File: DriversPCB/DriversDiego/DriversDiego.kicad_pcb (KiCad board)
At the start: 2 copper layers, 100 x 60 mm, 35 parts, among them IC1 DRV8411PWPR, IC2 DRV8411PWPR, IC3 DRV8411PWPR, J1 TB0012-508-02GR, J10 TB0012-508-02GR, J11 TB0012-508-02GR, J12 TB0012-508-02GR, J13 TB0012-508-02GR, J14 TB0012-508-02GR, J15 TB0012-508-02GR, J16 TB0012-508-02GR, J17 TB0012-508-02GR, J18 TB0012-508-02GR, J19 TB0012-508-02GR, J2 TB0012-508-02GR, J3 TB0012-508-02GR, J4 TB0012-508-02GR, J5 TB0012-508-02GR, J6 TB0012-508-02GR, J7 TB0012-508-02GR, J8 TB0012-508-02GR, J9 TB0012-508-02GR, U1 DRV8871DDA

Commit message: Zona cobre...
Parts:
- C1: footprint WCAP-CSGP_0805_H1.25:WCAP-CSGP_0805_H1.25_R -> Kicad_TitoSync_Footprints:WCAP-CSGP_0805_H1.25_R
- C3: footprint CL21B106KOQNFNE:CAPC2012X140N -> Kicad_TitoSync_Footprints:CAPC2012X140N
- IC1, IC2, IC3: footprint DRV8411PWPR:PWP0016C-IPC_A -> Kicad_TitoSync_Footprints:PWP0016C-IPC_A
- moved J14 93.2 mm to (115.0, 156.5), turned to 0 degrees
- moved J9 89.5 mm to (106.0, 133.0), turned to 90 degrees
- moved J15 80.6 mm to (193.5, 149.5), turned to -90 degrees
- moved J8 79.9 mm to (119.0, 104.5), turned to 0 degrees
- moved J19 76.2 mm to (180.0, 155.5), turned to 180 degrees
- moved J10 74.7 mm to (131.5, 104.0), turned to 0 degrees
- moved J6 73.2 mm to (128.0, 155.5)
- moved J4 63.2 mm to (106.5, 120.5), turned to -90 degrees
- moved J18 62.4 mm to (167.0, 155.5)
- moved J16 56.1 mm to (193.5, 137.0), turned to -90 degrees
- moved J5 55.9 mm to (154.0, 155.5), turned to 0 degrees
- moved J17 51.7 mm to (141.0, 155.5), turned to 0 degrees
- moved C3 51.6 mm to (114.6, 122.1), turned to -90 degrees
- moved J12 50.0 mm to (193.5, 124.0), turned to -90 degrees
- moved J11 48.6 mm to (169.5, 105.5)
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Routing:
- net Net-(IC1-VM): track 178.7 -> 104.2 mm, vias 0 -> 6
- net Net-(IC1-SLEEP_N): track 79.0 -> 11.6 mm
- net Net-(IC1-AOUT2): track 55.8 -> 20.4 mm
- net Net-(IC2-SLEEP_N): track 79.6 -> 49.1 mm, vias 0 -> 3
- net Net-(U1-OUT1): track 24.1 -> 53.4 mm, vias 0 -> 1
- net Net-(IC1-BOUT1): track 65.2 -> 39.2 mm, vias 0 -> 1
- net Net-(IC1-BOUT2): track 59.0 -> 33.6 mm, vias 0 -> 1
- net Net-(IC3-AIN2): track 13.9 -> 38.5 mm, vias 0 -> 1
- net Net-(IC2-BOUT1): track 23.9 -> 46.9 mm, vias 0 -> 1
- net Net-(U1-OUT2): track 28.8 -> 51.7 mm, vias 0 -> 2
- net Net-(IC3-SLEEP_N): track 58.8 -> 36.1 mm, vias 0 -> 3
- net Net-(IC3-AIN1): track 15.7 -> 36.1 mm, vias 0 -> 1
- net Net-(IC1-FAULT_N): track 44.9 -> 24.7 mm, vias 0 -> 1
- net Net-(IC3-AOUT2): track 27.0 -> 46.5 mm
- net Net-(IC1-BIN1): track 42.6 -> 24.3 mm
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- added copper zone on B.Cu, net GND

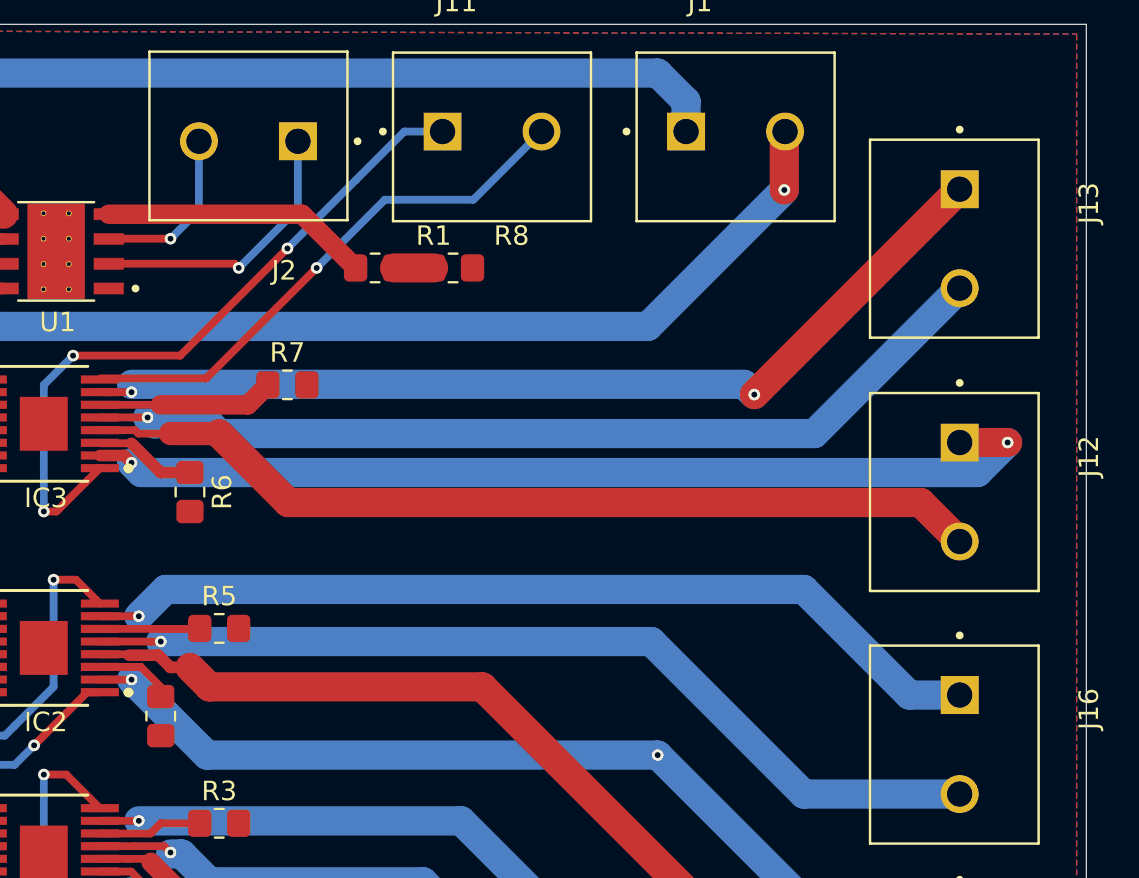
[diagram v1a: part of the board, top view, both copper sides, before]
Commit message: Driver PCB complete
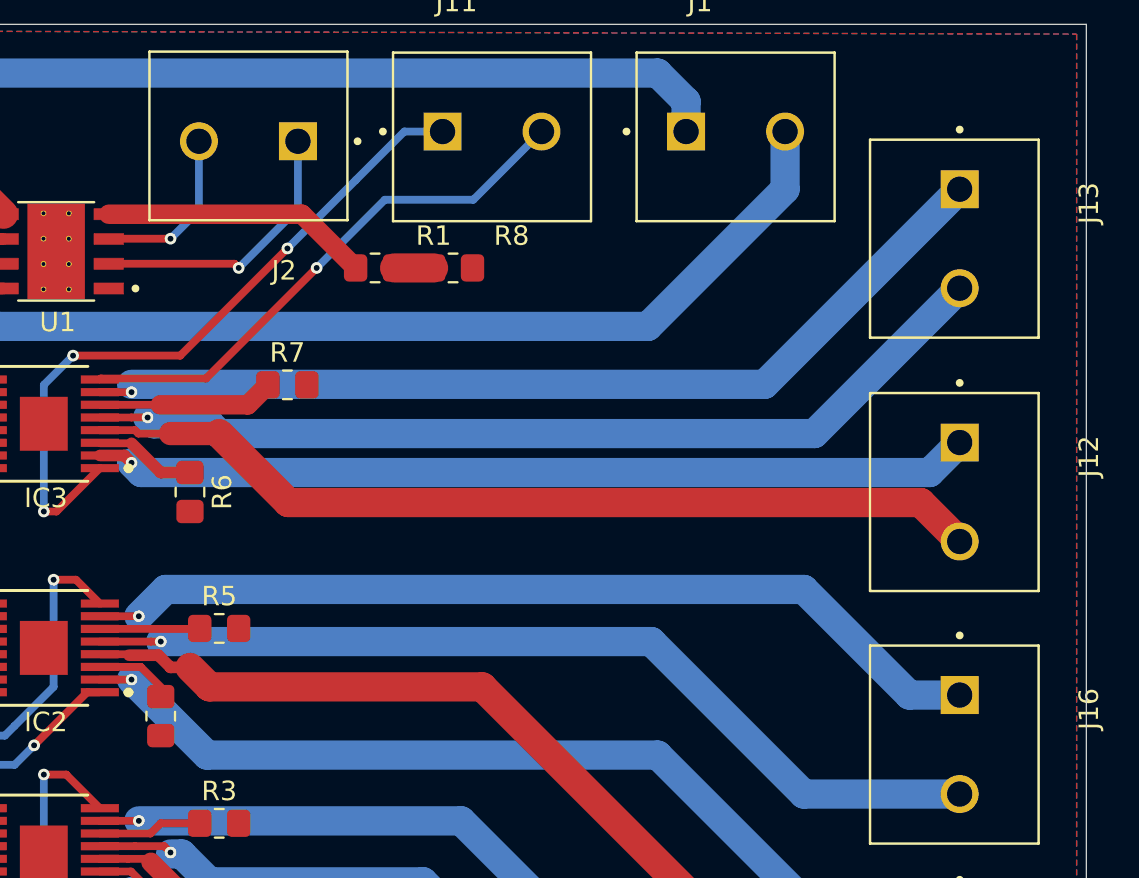
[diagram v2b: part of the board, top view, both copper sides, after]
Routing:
- net Net-(IC3-AOUT1): track 50.1 -> 45.1 mm, vias 2 -> 1
- net Net-(IC3-BOUT1): track 48.7 -> 48.3 mm, vias 2 -> 1
- net Net-(U1-OUT2): vias 2 -> 1
- net Net-(IC2-AOUT1): vias 2 -> 1
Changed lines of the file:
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@@
 			(drillshape 0)
 			(scaleselection 1)
-			(outputdirectory "./")
+			(outputdirectory "E:/GitRepos/TitoSync/DriversPCB/Gerbers/")
 		)
 	)
@@
 		(net 30)
 	)
-	(via
-		(at 178 137.5)
-		(size 0.6)
-		(drill 0.3)
-		(layers "F.Cu" "B.Cu")
-		(net 30)
-	)
 	(segment
 		(start 154.875 137.5)
@@
 	)
 	(segment
-		(start 195.96 121.46)
-		(end 196 121.5)
-		(width 0.2)
-		(layer "F.Cu")
-		(net 38)
-	)
-	(segment
 		(start 150.625 122.125)
 		(end 151 122.5)
@@
 	)
 	(segment
-		(start 193.5 121.46)
-		(end 195.96 121.46)
-		(width 1.5)
-		(layer "F.Cu")
-		(net 38)
-	)
-	(segment
 		(start 149.37538 122.125)
 		(end 150.625 122.125)
@@
 		(net 38)
 	)
-	(via
-		(at 195.96 121.46)
-		(size 0.6)
-		(drill 0.3)
-		(layers "F.Cu" "B.Cu")
-		(net 38)
-	)
 	(segment
-		(start 194.42 123)
+		(start 191.96 123)
 		(end 151.5 123)
 		(width 1.5)
@@
 	)
 	(segment
-		(start 195.96 121.46)
-		(end 194.42 123)
+		(start 193.5 121.46)
+		(end 191.96 123)
 		(width 1.5)
 		(layer "B.Cu")
@@
 	)
 	(segment
-		(start 193.5 108.46)
-		(end 182.96 119)
-		(width 1.5)
-		(layer "F.Cu")
-		(net 41)
-	)
-	(segment
 		(start 149.37538 118.875)
 		(end 151 118.875)
@@
 		(net 41)
 	)
-	(via
-		(at 182.96 119)
-		(size 0.6)
-		(drill 0.3)
-		(layers "F.Cu" "B.Cu")
-		(net 41)
-	)
 	(segment
-		(start 182.434 118.474)
-		(end 151 118.474)
+		(start 193.5 108.46)
+		(end 183.486 118.474)
 		(width 1.5)
 		(layer "B.Cu")
@@
 	)
 	(segment
-		(start 182.96 119)
-		(end 182.434 118.474)
+		(start 183.486 118.474)
+		(end 151 118.474)
 		(width 1.5)
 		(layer "B.Cu")
@@
 	)
 	(segment
-		(start 184.5 105.54)
-		(end 184.5 108.5)
-		(width 1.5)
-		(layer "F.Cu")
-		(net 46)
-	)
-	(segment
 		(start 184.54 105.5)
 		(end 184.5 105.54)
@@
 	)
 	(via
-		(at 184.5 108.5)
-		(size 0.6)
-		(drill 0.3)
-		(layers "F.Cu" "B.Cu")
-		(net 46)
-	)
-	(via
 		(at 142 113.555)
 		(size 0.6)
@@
 	)
 	(segment
+		(start 142 113.555)
+		(end 143.945 115.5)
+		(width 1.5)
+		(layer "B.Cu")
+		(net 46)
+	)
+	(segment
 		(start 177.5 115.5)
-		(end 184.5 108.5)
+		(end 184.54 108.46)
 		(width 1.5)
 		(layer "B.Cu")
@@
 	)
 	(segment
-		(start 142 113.555)
-		(end 143.945 115.5)
+		(start 184.54 108.46)
+		(end 184.54 105.5)
 		(width 1.5)
 		(layer "B.Cu")

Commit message: Last PCB revision
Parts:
- removed J1, J10, J11, J12, J13, J14, J15, J16, J17, J18, J19, J2, J4, J5, J6, J7, J8, J9: TB0012-508-02GR, Kicad_TitoSync_Footprints:SAMESKY_TB0012-508-02GR
- added C5: 10uF, Capacitor_SMD:C_1206_3216Metric, F.Cu at (125.1, 108.5)
- added C6: 1uF, Capacitor_SMD:C_0603_1608Metric, F.Cu at (127.8, 108.5)
- added C7: 0.1uF, Capacitor_SMD:C_0402_1005Metric, F.Cu at (133.1, 129.0)
- added C8: 0.1uF, Capacitor_SMD:C_0402_1005Metric, F.Cu at (133.1, 143.0)
- added DC_IN1: DC_CTRL, Connector_PinHeader_2.54mm:PinHeader_1x02_P2.54mm_Vertical, F.Cu at (149.9, 153.6)
- added GND: Ground Pins, Connector_PinHeader_2.54mm:PinHeader_1x02_P2.54mm_Vertical, F.Cu at (102.3, 119.1)
- added POWER_IN: POWER_IN, TerminalBlock_MetzConnect:TerminalBlock_MetzConnect_Type094_RT03502HBLU_1x02_P5.00mm_Horizontal, F.Cu at (104.8, 106.4)
- added R10: 1k, Resistor_SMD:R_0805_2012Metric_Pad1.20x1.40mm_HandSolder, F.Cu at (140.9, 137.3)
- added R9: 100m, Resistor_SMD:R_1206_3216Metric, F.Cu at (135.5, 146.2)
- added STP1: STP1_CTRL, Connector_PinHeader_2.54mm:PinHeader_1x06_P2.54mm_Vertical, F.Cu at (102.2, 143.9)
- added STP1_OUT1: STP1_OUT, Connector_PinHeader_2.54mm:PinHeader_1x04_P2.54mm_Vertical, F.Cu at (149.8, 117.0)
- added STP2: STP2_CTRL, Connector_PinHeader_2.54mm:PinHeader_1x06_P2.54mm_Vertical, F.Cu at (107.2, 143.9)
- added STP2_OUT1: STP2_OUT, Connector_PinHeader_2.54mm:PinHeader_1x04_P2.54mm_Vertical, F.Cu at (149.8, 131.0)
- added STP3: STP3_CTRL, Connector_PinHeader_2.54mm:PinHeader_1x06_P2.54mm_Vertical, F.Cu at (112.1, 143.9)
- added STP3_OUT1: STP3_OUT, Connector_PinHeader_2.54mm:PinHeader_1x04_P2.54mm_Vertical, F.Cu at (149.8, 145.0)
- C1: value WCAP-CSGP_0805_H1.25 -> 0.1uF; footprint Kicad_TitoSync_Footprints:WCAP-CSGP_0805_H1.25_R -> Capacitor_SMD:C_0402_1005Metric
- C2: value 500R15Y104MV4T -> 0.1uF; footprint Kicad_TitoSync_Footprints:CAPC2012X127N -> Capacitor_SMD:C_0402_1005Metric
- C3: value CL21B106KOQNFNE -> 47uF; footprint Kicad_TitoSync_Footprints:CAPC2012X140N -> Capacitor_SMD:CP_Elec_6.3x5.4
- C4: value 500R15Y104MV4T -> 10uF; footprint Kicad_TitoSync_Footprints:EXV-9B_KEM -> Capacitor_SMD:C_1206_3216Metric
- IC1, IC2, IC3: footprint Kicad_TitoSync_Footprints:PWP0016C-IPC_A -> Package_SO:HTSSOP-16-1EP_4.4x5mm_P0.65mm_EP3.4x5mm_Mask2.66x2.46mm
- J3: value TB0012-508-02GR -> DC_OUT; footprint Kicad_TitoSync_Footprints:SAMESKY_TB0012-508-02GR -> TerminalBlock_MetzConnect:TerminalBlock_MetzConnect_Type094_RT03502HBLU_1x02_P5.00mm_Horizontal
- R1: value R -> 30k
- R2, R3, R5, R6, R8: value R -> 100m; footprint Resistor_SMD:R_0805_2012Metric_Pad1.20x1.40mm_HandSolder -> Resistor_SMD:R_1206_3216Metric
- R4, R7: value R -> 1k
- moved C1 46.4 mm to (136.3, 151.7), turned to 180 degrees
- moved R1 45.3 mm to (139.9, 151.2)
- moved J3 44.3 mm to (104.8, 151.7)
- moved U1 44.2 mm to (138.0, 154.9)
- moved R8 43.4 mm to (140.1, 146.2)
- moved R2 31.4 mm to (140.2, 118.1), turned to 0 degrees
- moved R3 30.3 mm to (135.7, 118.1)
- moved IC1 29.8 mm to (138.0, 114.0)
- moved R4 28.6 mm to (141.0, 109.3), turned to 90 degrees
- moved IC3 23.1 mm to (138.0, 142.0)
- moved R6 19.8 mm to (135.9, 132.1), turned to 0 degrees
- moved C2 19.2 mm to (133.2, 115.0), turned to 180 degrees
- moved R7 18.7 mm to (140.9, 123.3), turned to 90 degrees
- moved C4 16.8 mm to (122.2, 108.5)
- moved R5 15.0 mm to (140.5, 132.1)
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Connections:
- C1 pad 1: Net-(U1-VM) -> GND
- C1 pad 2: GND -> VM
- C2 pad 1: Net-(U1-VM) -> GND
- C2 pad 2: GND -> VM
- C3 pad 1: Net-(IC1-VM) -> VM
- C4 pad 1: Net-(IC1-VM) -> GND
- C4 pad 2: GND -> VM
- IC1 pad 1: Net-(IC1-SLEEP_N) -> SLEEP_STP1
- IC1 pad 10: Net-(IC1-BIN2) -> BIN2_STP1
- IC1 pad 12: Net-(IC1-VM) -> VM
- IC1 pad 15: Net-(IC1-AIN2) -> AIN2_STP1
- IC1 pad 16: Net-(IC1-AIN1) -> AIN1_STP1
- IC1 pad 2: Net-(IC1-AOUT1) -> AOUT1_STP1
- IC1 pad 4: Net-(IC1-AOUT2) -> AOUT2_STP1
- IC1 pad 5: Net-(IC1-BOUT2) -> BOUT2_STP1
- IC1 pad 7: Net-(IC1-BOUT1) -> BOUT1_STP1
- IC1 pad 8: Net-(IC1-FAULT_N) -> FAULT_STP1
- IC1 pad 9: Net-(IC1-BIN1) -> BIN1_STP1
- IC2 pad 1: Net-(IC2-SLEEP_N) -> SLEEP_STP2
- IC2 pad 10: Net-(IC2-BIN2) -> BIN2_STP2
- IC2 pad 12: Net-(IC1-VM) -> VM
- IC2 pad 15: Net-(IC2-AIN2) -> AIN2_STP2
- IC2 pad 16: Net-(IC2-AIN1) -> AIN1_STP2
- IC2 pad 2: Net-(IC2-AOUT1) -> AOUT1_STP2
- IC2 pad 4: Net-(IC2-AOUT2) -> AOUT2_STP2
- IC2 pad 5: Net-(IC2-BOUT2) -> BOUT2_STP2
- IC2 pad 7: Net-(IC2-BOUT1) -> BOUT1_STP2
- IC2 pad 8: Net-(IC2-FAULT_N) -> FAULT_STP2
- IC2 pad 9: Net-(IC2-BIN1) -> BIN1_STP2
- IC3 pad 1: Net-(IC3-SLEEP_N) -> SLEEP_STP3
- IC3 pad 10: Net-(IC3-BIN2) -> BIN2_STP3
- IC3 pad 12: Net-(IC1-VM) -> VM
- IC3 pad 15: Net-(IC3-AIN2) -> AIN2_STP3
- IC3 pad 16: Net-(IC3-AIN1) -> AIN1_STP3
- IC3 pad 2: Net-(IC3-AOUT1) -> AOUT1_STP3
- IC3 pad 4: Net-(IC3-AOUT2) -> AOUT2_STP3
- IC3 pad 5: Net-(IC3-BOUT2) -> BOUT2_STP3
- IC3 pad 7: Net-(IC3-BOUT1) -> BOUT1_STP3
- IC3 pad 8: Net-(IC3-FAULT_N) -> FAULT_STP3
- IC3 pad 9: Net-(IC3-BIN1) -> BIN1_STP3
- J3 pad 1: Net-(U1-VM) -> OUT1_DC
- J3 pad 2: GND -> OUT2_DC
- R1 pad 1: Net-(U1-ILIM) -> GND
- R1 pad 2: Net-(R1-Pad2) -> Net-(U1-ILIM)
- R2 pad 1: Net-(IC1-AISEN) -> GND
- R2 pad 2: GND -> Net-(IC1-AISEN)
- R4 pad 1: Net-(IC2-AISEN) -> FAULT_STP1
- R4 pad 2: GND -> SLEEP_STP1
- R5 pad 1: Net-(IC2-BISEN) -> GND
- R5 pad 2: GND -> Net-(IC2-AISEN)
- R6 pad 1: Net-(IC3-AISEN) -> Net-(IC2-BISEN)
- R7 pad 1: Net-(IC3-BISEN) -> FAULT_STP2
- R7 pad 2: GND -> SLEEP_STP2
- R8 pad 1: Net-(R1-Pad2) -> GND
- R8 pad 2: GND -> Net-(IC3-AISEN)
- U1 pad 2: Net-(U1-IN2) -> IN2_DC
- U1 pad 3: Net-(U1-IN1) -> IN1_DC
- U1 pad 5: Net-(U1-VM) -> VM
- U1 pad 6: Net-(U1-OUT1) -> OUT1_DC
- U1 pad 8: Net-(U1-OUT2) -> OUT2_DC
- U1 pad 9: (no net) -> GND
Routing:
- net Net-(IC1-VM): track 104.2 -> 0.00 mm, vias 6 -> 0
- net FAULT_STP1: track 0.00 -> 64.7 mm, vias 0 -> 1
- net AIN1_STP2: track 0.00 -> 62.4 mm, vias 0 -> 1
- net BIN1_STP2: track 0.00 -> 58.9 mm, vias 0 -> 1
- net SLEEP_STP1: track 0.00 -> 58.8 mm, vias 0 -> 2
- net BIN2_STP2: track 0.00 -> 53.5 mm, vias 0 -> 1
- net Net-(U1-OUT1): track 53.4 -> 0.00 mm, vias 1 -> 0
- net BIN1_STP1: track 0.00 -> 53.4 mm, vias 0 -> 1
- net SLEEP_STP2: track 0.00 -> 53.1 mm, vias 0 -> 2
- net Net-(IC2-FAULT_N): track 53.1 -> 0.00 mm, vias 3 -> 0
- net Net-(IC2-AOUT2): track 52.3 -> 0.00 mm
- net Net-(U1-OUT2): track 51.7 -> 0.00 mm, vias 1 -> 0
- net AIN1_STP1: track 0.00 -> 51.0 mm, vias 0 -> 1
- net Net-(IC2-AOUT1): track 49.6 -> 0.00 mm, vias 1 -> 0
- net Net-(IC2-SLEEP_N): track 49.1 -> 0.00 mm, vias 3 -> 0
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- added copper zone on B.Cu, net AOUT1_STP1
- added copper zone on F.Cu, net AOUT1_STP1
- added copper zone on B.Cu, net AOUT1_STP2
- added copper zone on F.Cu, net AOUT1_STP2
- added copper zone on B.Cu, net AOUT1_STP3
- added copper zone on F.Cu, net AOUT1_STP3
- added copper zone on B.Cu, net AOUT2_STP1
- added copper zone on F.Cu, net AOUT2_STP1
- added copper zone on B.Cu, net AOUT2_STP2
- added copper zone on F.Cu, net AOUT2_STP2
- added copper zone on B.Cu, net AOUT2_STP3
- added copper zone on F.Cu, net AOUT2_STP3
- added copper zone on B.Cu, net BOUT1_STP1
- added copper zone on F.Cu, net BOUT1_STP1
- added copper zone on B.Cu, net BOUT1_STP2
- added copper zone on F.Cu, net BOUT1_STP2
- added copper zone on B.Cu, net BOUT1_STP3
- added copper zone on F.Cu, net BOUT1_STP3
- added copper zone on B.Cu, net BOUT2_STP1
- added copper zone on F.Cu, net BOUT2_STP1
- added copper zone on B.Cu, net BOUT2_STP2
- added copper zone on F.Cu, net BOUT2_STP2
- added copper zone on B.Cu, net BOUT2_STP3
- added copper zone on F.Cu, net BOUT2_STP3
- added copper zone on F.Cu, net IN1_DC
- added copper zone on F.Cu, net IN2_DC
- added copper zone on B.Cu, net OUT1_DC
- added copper zone on F.Cu, net OUT1_DC
- added copper zone on B.Cu, net OUT2_DC
- added copper zone on F.Cu, net OUT2_DC
- added copper zone on B.Cu, net VM
- added copper zone on F.Cu, net VM
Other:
- board size 100 x 60 mm -> 53.6 x 60 mm
- copper layers 2 -> 4
- board text added: "A1"
- board text added: "A2"
- board text added: "AIN1"
- board text added: "AIN2"
- board text added: "B1"
- board text added: "B2"
- board text added: "BIN1"
- board text added: "BIN2"
- board text added: "DC_OUT"
- board text added: "FAULT"
- board text added: "IN1"
- board text added: "IN2"
- board text added: "SLEEP"

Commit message: Final PCB
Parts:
- added G***: LOGO, LOGO, F.Cu at (112.5, 121.3)
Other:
- board text added: "N_FAULT"
- board text removed: "FAULT"
